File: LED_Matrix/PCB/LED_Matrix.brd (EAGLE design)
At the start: 31.8 x 31.8 mm, 9 parts, among them J1 NONE, J2 HEADER-1X8, J3 HEADER-1X8, P1 NONE, U1 ATTINY48, U2 ULN2803AFWG

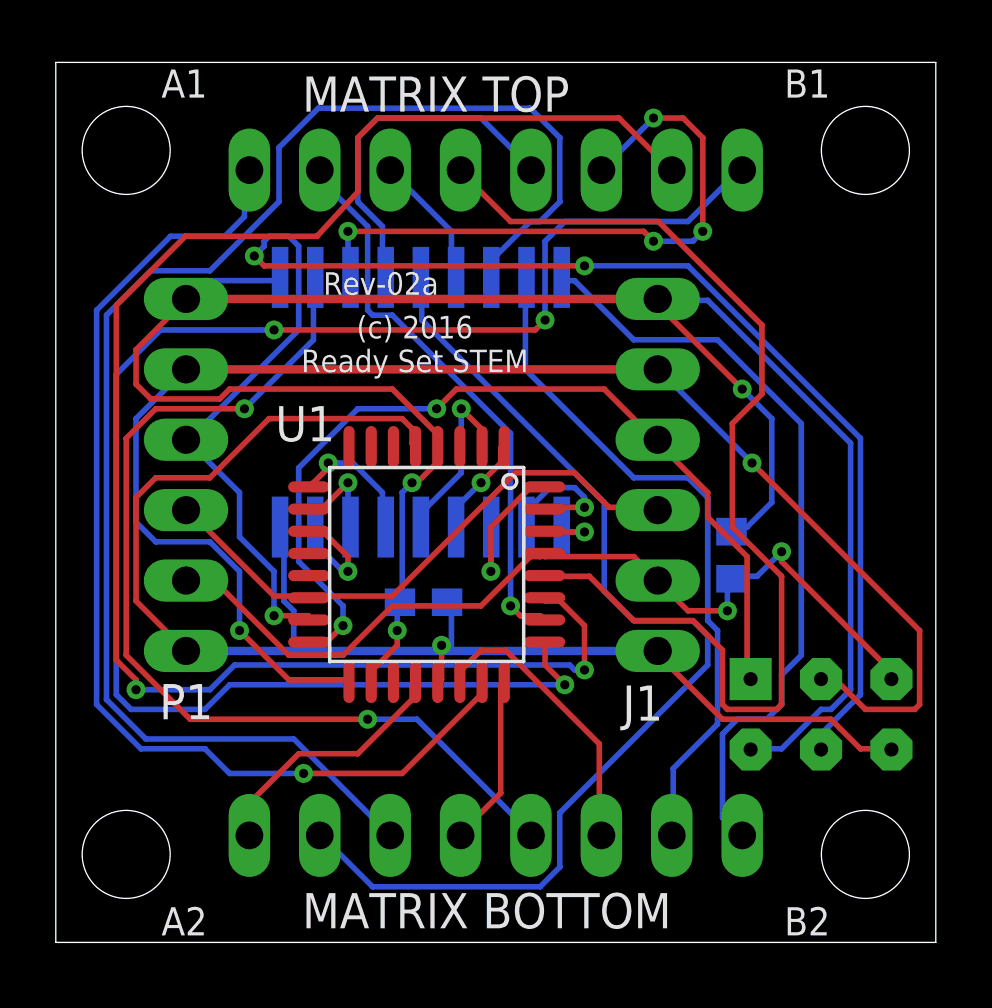
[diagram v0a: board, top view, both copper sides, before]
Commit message: LED Matrix - board size now 1.24 x 1.24
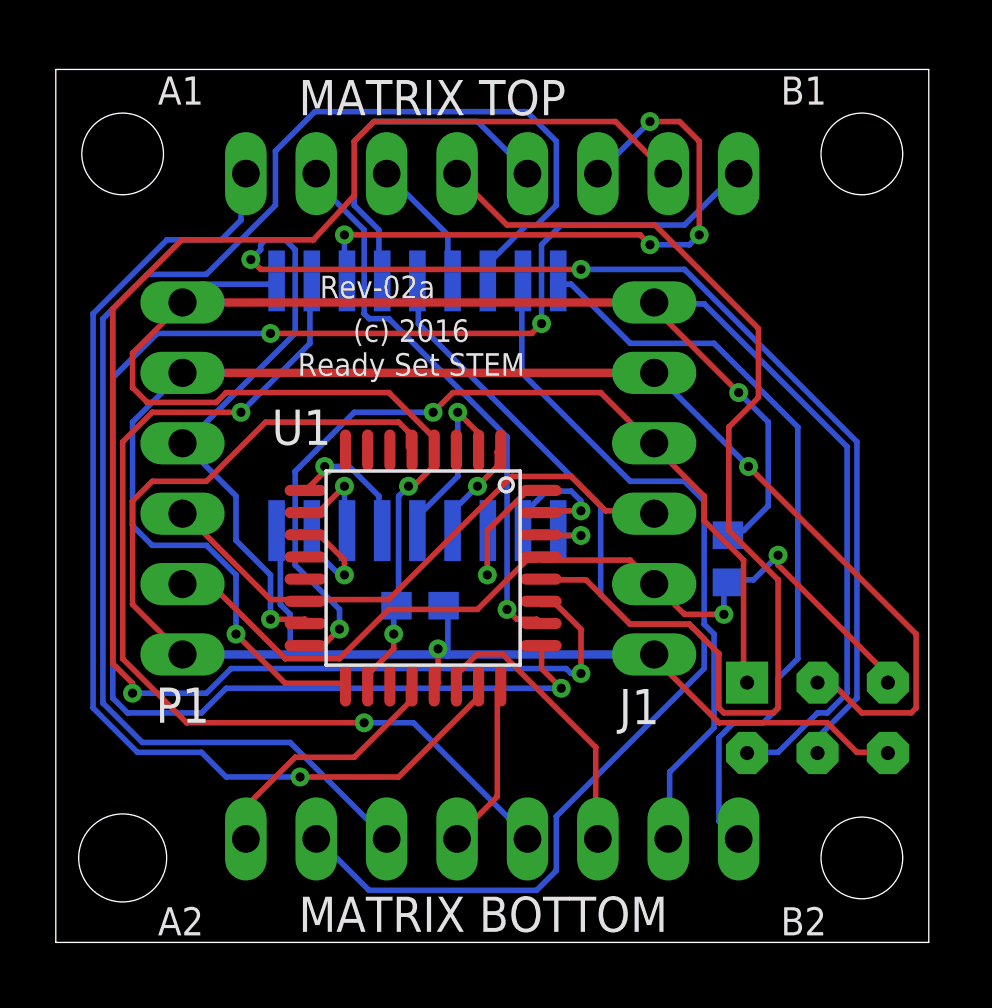
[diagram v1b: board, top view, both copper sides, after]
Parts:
- moved J2 0.18 mm to (15.7, 27.7)
- moved U2 0.18 mm to (18.1, 14.9)
- moved C1 0.18 mm to (13.1, 12.1)
- moved U1 0.18 mm to (13.3, 13.5)
- moved J3 0.18 mm to (15.7, 3.73)
- moved P1 0.18 mm to (4.57, 16.7)
- moved J1 0.18 mm to (21.6, 16.7)
- moved PROG 0.18 mm to (27.5, 8.10)
- moved R1 0.18 mm to (24.3, 13.8)
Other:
- board size 31.8 x 31.8 mm -> 31.5 x 31.5 mm

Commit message: LED Matrix - hole sizes
Smaller mouting holes, to give a better safe distance to the board edge now that the board is
slightly smaller (1.24).  Should still fit #4 screws, albeit snugly.

Bigger PROG pad holes.

Fixed DRC issues
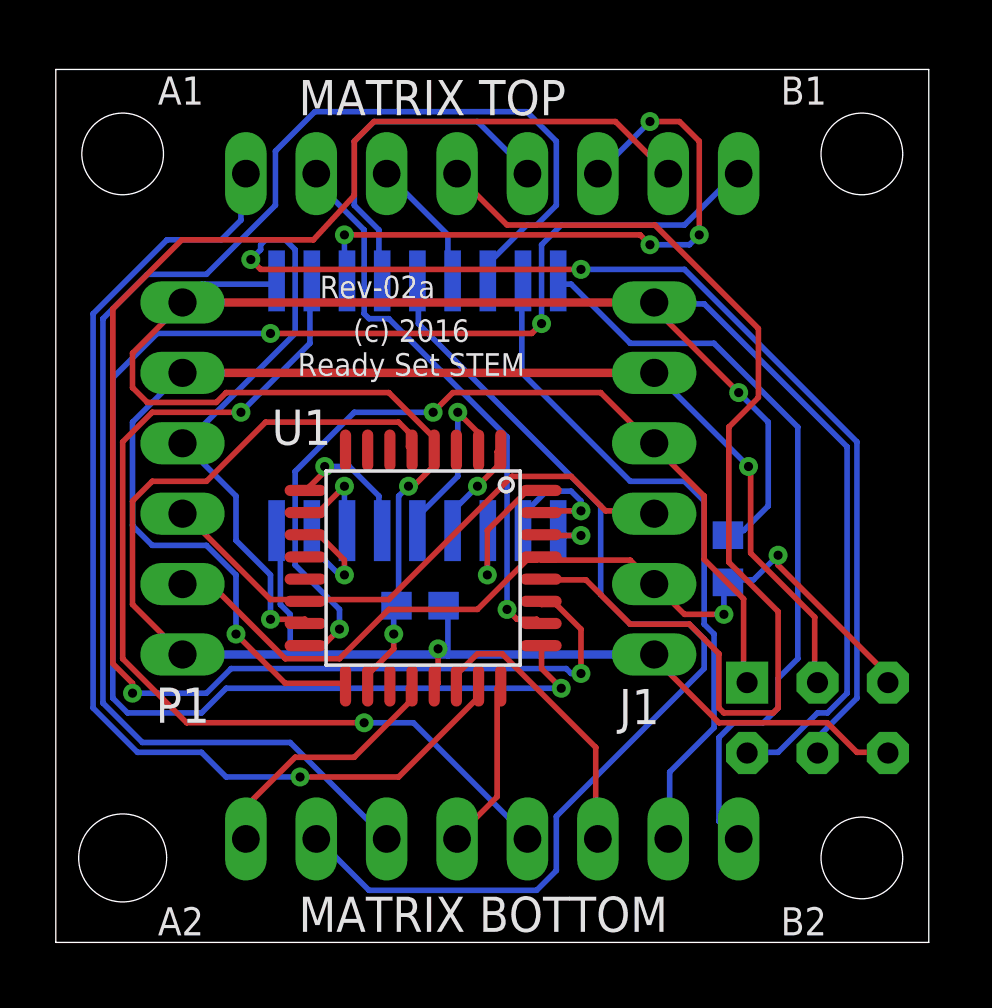
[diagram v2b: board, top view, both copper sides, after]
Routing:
- net SCK: track 54.8 -> 48.3 mm

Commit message: reduced board to 1.23x1.23, and mounting holes to 110 mils
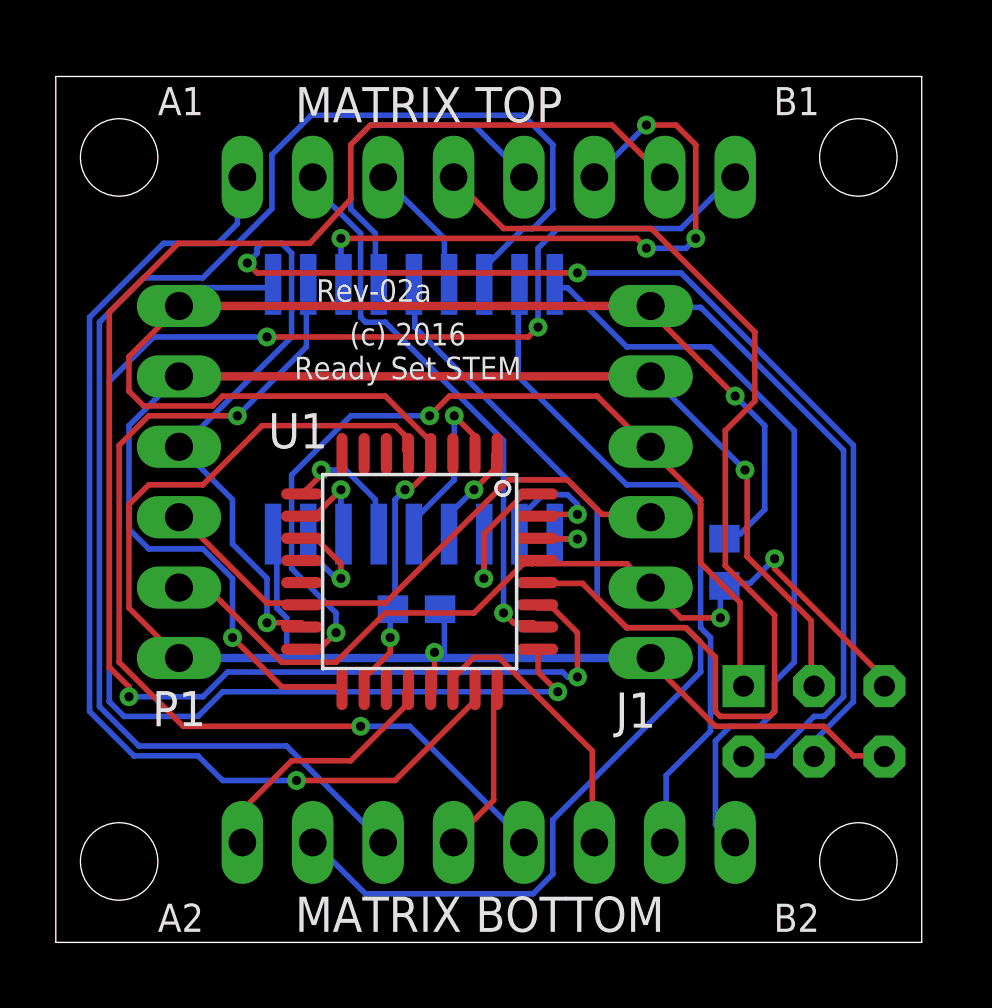
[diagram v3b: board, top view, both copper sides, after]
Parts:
- moved PROG 0.18 mm to (27.4, 7.98)
- moved R1 0.18 mm to (24.1, 13.7)
- moved P1 0.18 mm to (4.45, 16.6)
- moved J1 0.18 mm to (21.5, 16.6)
- moved C1 0.18 mm to (13.0, 12.0)
- moved J3 0.18 mm to (15.6, 3.61)
- moved J2 0.18 mm to (15.6, 27.6)
- moved U1 0.18 mm to (13.1, 13.4)
- moved U2 0.18 mm to (18.0, 14.7)
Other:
- board size 31.5 x 31.5 mm -> 31.2 x 31.2 mm

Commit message: led matrix - moved chaining connectors in by 10 mils
This matches previous change to take 10 mils off of each edge
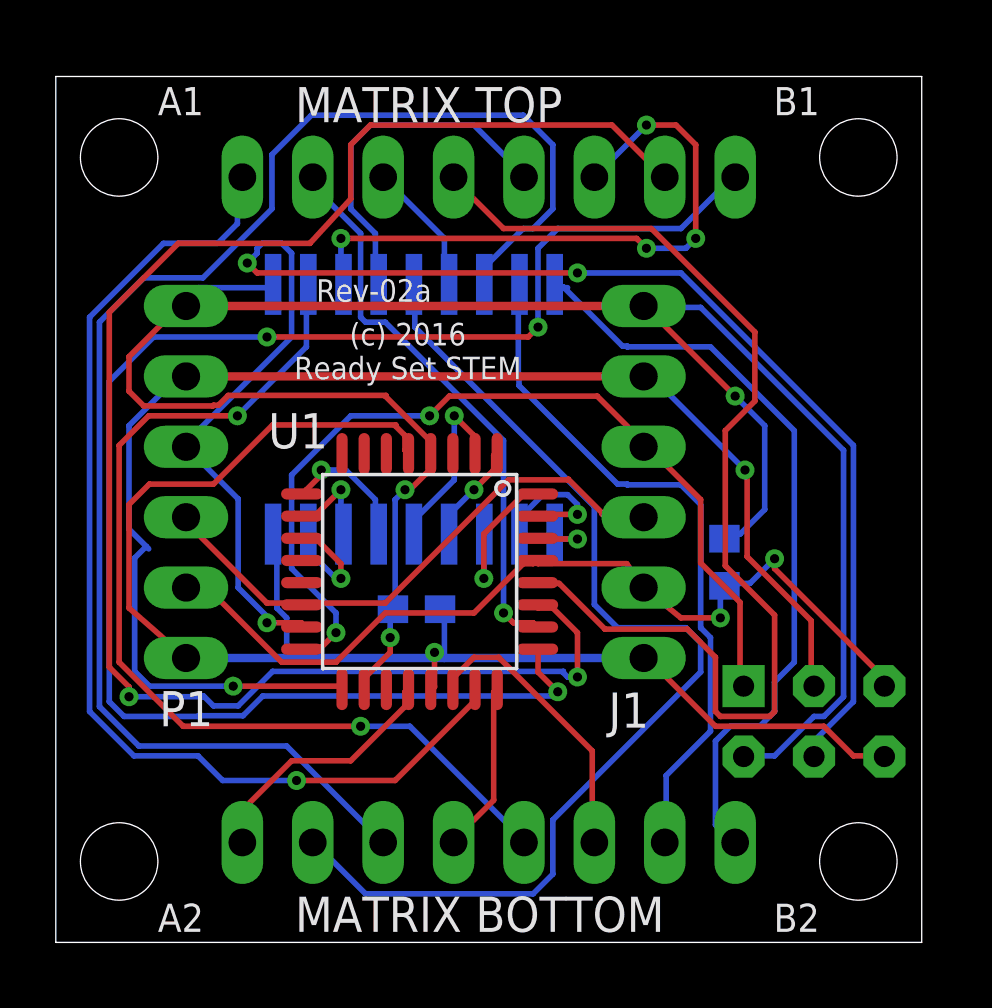
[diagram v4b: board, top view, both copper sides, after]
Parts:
- moved J1 0.25 mm to (21.2, 16.6)
- moved P1 0.25 mm to (4.70, 16.6)
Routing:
- net SCK: track 48.3 -> 50.4 mm
- net CS: track 20.7 -> 22.2 mm

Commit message: led matrix - rerouted weird via on GND trace
Probably not an issue, but better with via not on trace
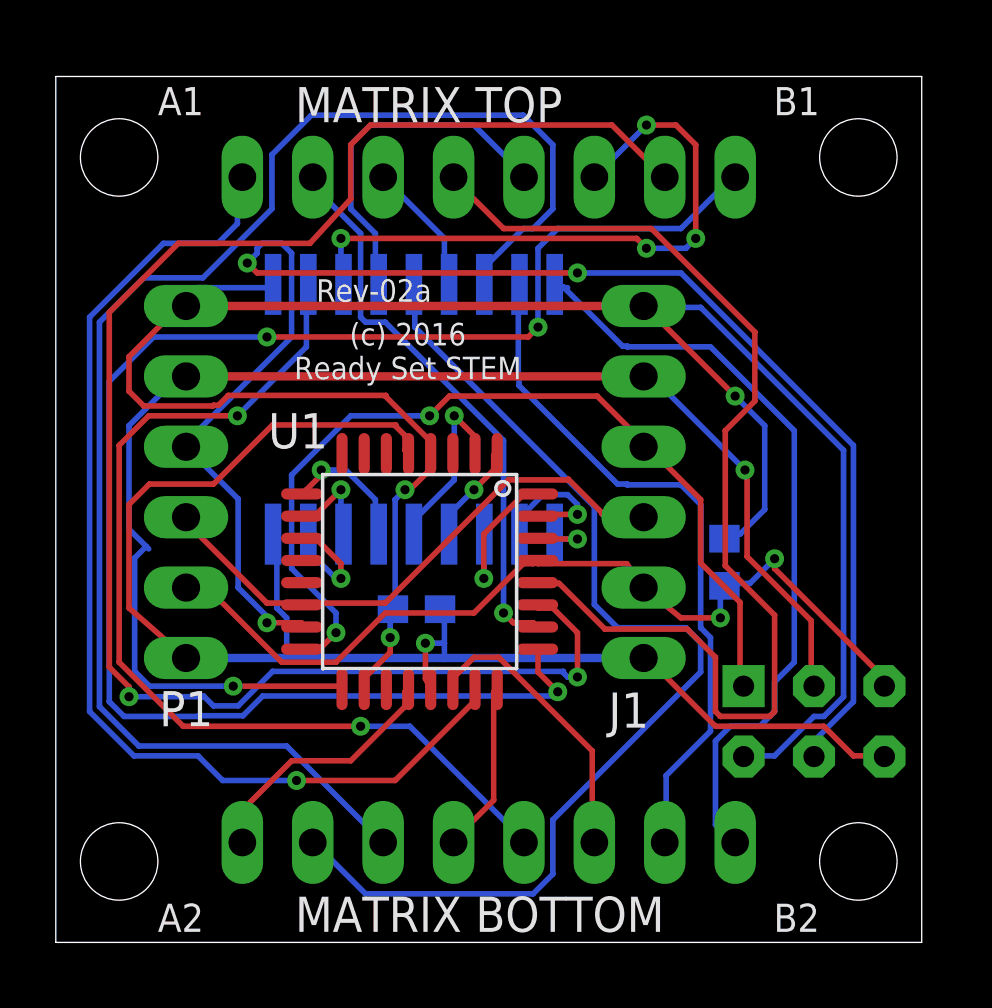
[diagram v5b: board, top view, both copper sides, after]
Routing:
- net GND: track 53.3 -> 54.1 mm
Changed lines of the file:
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@@
 <layer number="17" name="Pads" color="2" fill="1" visible="yes" active="yes"/>
 <layer number="18" name="Vias" color="2" fill="1" visible="yes" active="yes"/>
-<layer number="19" name="Unrouted" color="6" fill="1" visible="no" active="yes"/>
-<layer number="20" name="Dimension" color="15" fill="1" visible="no" active="yes"/>
+<layer number="19" name="Unrouted" color="6" fill="1" visible="yes" active="yes"/>
+<layer number="20" name="Dimension" color="15" fill="1" visible="yes" active="yes"/>
 <layer number="21" name="tPlace" color="7" fill="1" visible="no" active="yes"/>
 <layer number="22" name="bPlace" color="7" fill="1" visible="no" active="yes"/>
-<layer number="23" name="tOrigins" color="15" fill="1" visible="no" active="yes"/>
-<layer number="24" name="bOrigins" color="15" fill="1" visible="no" active="yes"/>
+<layer number="23" name="tOrigins" color="15" fill="1" visible="yes" active="yes"/>
+<layer number="24" name="bOrigins" color="15" fill="1" visible="yes" active="yes"/>
 <layer number="25" name="tNames" color="7" fill="1" visible="no" active="yes"/>
 <layer number="26" name="bNames" color="7" fill="1" visible="no" active="yes"/>
 <layer number="27" name="tValues" color="7" fill="1" visible="no" active="yes"/>
 <layer number="28" name="bValues" color="7" fill="1" visible="no" active="yes"/>
-<layer number="29" name="tStop" color="7" fill="3" visible="no" active="yes"/>
-<layer number="30" name="bStop" color="7" fill="6" visible="no" active="yes"/>
-<layer number="31" name="tCream" color="7" fill="4" visible="no" active="yes"/>
-<layer number="32" name="bCream" color="7" fill="5" visible="no" active="yes"/>
-<layer number="33" name="tFinish" color="6" fill="3" visible="no" active="yes"/>
-<layer number="34" name="bFinish" color="6" fill="6" visible="no" active="yes"/>
-<layer number="35" name="tGlue" color="7" fill="4" visible="no" active="yes"/>
-<layer number="36" name="bGlue" color="7" fill="5" visible="no" active="yes"/>
+<layer number="29" name="tStop" color="7" fill="3" visible="yes" active="yes"/>
+<layer number="30" name="bStop" color="7" fill="6" visible="yes" active="yes"/>
+<layer number="31" name="tCream" color="7" fill="4" visible="yes" active="yes"/>
+<layer number="32" name="bCream" color="7" fill="5" visible="yes" active="yes"/>
+<layer number="33" name="tFinish" color="6" fill="3" visible="yes" active="yes"/>
+<layer number="34" name="bFinish" color="6" fill="6" visible="yes" active="yes"/>
+<layer number="35" name="tGlue" color="7" fill="4" visible="yes" active="yes"/>
+<layer number="36" name="bGlue" color="7" fill="5" visible="yes" active="yes"/>
 <layer number="37" name="tTest" color="7" fill="1" visible="no" active="yes"/>
 <layer number="38" name="bTest" color="7" fill="1" visible="no" active="yes"/>
@@
 <layer number="42" name="bRestrict" color="1" fill="10" visible="no" active="yes"/>
 <layer number="43" name="vRestrict" color="2" fill="10" visible="no" active="yes"/>
-<layer number="44" name="Drills" color="7" fill="1" visible="no" active="yes"/>
-<layer number="45" name="Holes" color="7" fill="1" visible="no" active="yes"/>
-<layer number="46" name="Milling" color="3" fill="1" visible="no" active="yes"/>
+<layer number="44" name="Drills" color="7" fill="1" visible="yes" active="yes"/>
+<layer number="45" name="Holes" color="7" fill="1" visible="yes" active="yes"/>
+<layer number="46" name="Milling" color="3" fill="1" visible="yes" active="yes"/>
 <layer number="47" name="Measures" color="7" fill="1" visible="no" active="yes"/>
 <layer number="48" name="Document" color="7" fill="1" visible="no" active="yes"/>
@@
 <contactref element="J1" pad="6"/>
 <wire x1="4.699" y1="10.2616" x2="8.3312" y2="10.2616" width="0.3048" layer="16"/>
-<wire x1="8.3312" y1="10.2616" x2="13.6652" y2="10.2616" width="0.3048" layer="16"/>
-<wire x1="13.6652" y1="10.2616" x2="14.0208" y2="10.2616" width="0.3048" layer="16"/>
+<wire x1="8.3312" y1="10.2616" x2="14.0208" y2="10.2616" width="0.3048" layer="16"/>
 <wire x1="14.0208" y1="10.2616" x2="21.209" y2="10.2616" width="0.3048" layer="16"/>
-<wire x1="14.0208" y1="10.2616" x2="14.0208" y2="11.8872" width="0.2032" layer="16"/>
+<wire x1="14.0208" y1="10.2616" x2="14.0208" y2="10.795" width="0.2032" layer="16"/>
+<wire x1="14.0208" y1="10.795" x2="14.0208" y2="11.8872" width="0.2032" layer="16"/>
 <wire x1="14.0208" y1="11.8872" x2="13.8642" y2="12.0216" width="0.2032" layer="16"/>
-<wire x1="13.6652" y1="10.4648" x2="13.6652" y2="9.2202" width="0.2032" layer="1"/>
-<wire x1="13.6652" y1="10.2616" x2="13.6652" y2="10.4648" width="0.2032" layer="16"/>
-<wire x1="13.6652" y1="9.2202" x2="13.527" y2="9.13" width="0.2032" layer="1"/>
 <wire x1="12.5984" y1="18.288" x2="12.5984" y2="17.7546" width="0.2032" layer="1"/>
 <wire x1="12.2428" y1="18.6436" x2="12.5984" y2="18.288" width="0.2032" layer="1"/>
@@
 <wire x1="4.699" y1="10.2616" x2="2.6416" y2="12.065" width="0.2032" layer="1"/>
 <wire x1="12.5984" y1="17.7546" x2="12.727" y2="17.63" width="0.2032" layer="1"/>
-<via x="13.6652" y="10.4648" extent="1-16" drill="0.3302"/>
 <contactref element="U2" pad="GND"/>
 <wire x1="7.9756" y1="12.065" x2="7.9756" y2="14.5542" width="0.2032" layer="16"/>
@@
 <wire x1="3.3782" y1="16.5354" x2="5.6896" y2="16.5354" width="0.2032" layer="1"/>
 <wire x1="12.2682" y1="18.669" x2="12.2428" y2="18.6436" width="0.2032" layer="1"/>
+<wire x1="13.335" y1="10.795" x2="13.335" y2="9.525" width="0.2032" layer="1"/>
+<wire x1="14.0208" y1="10.795" x2="13.335" y2="10.795" width="0.2032" layer="16"/>
+<wire x1="13.335" y1="9.525" x2="13.527" y2="9.13" width="0.2032" layer="1"/>
+<via x="13.335" y="10.795" extent="1-16" drill="0.3302"/>
 </signal>
 <signal name="SCK">
@@
 <contactref element="P1" pad="3"/>
 <wire x1="7.62" y1="11.5316" x2="8.8646" y2="11.5316" width="0.2032" layer="1"/>
-<wire x1="7.62" y1="13.1318" x2="7.62" y2="11.5316" width="0" layer="19" extent="1-16"/>
 <wire x1="8.8646" y1="11.5316" x2="8.877" y2="11.38" width="0.2032" layer="1"/>
 <wire x1="4.5974" y1="17.7546" x2="4.699" y2="17.8816" width="0.2032" layer="16"/>
